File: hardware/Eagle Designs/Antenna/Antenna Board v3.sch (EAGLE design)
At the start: 12 parts, among them J10 U.FL-R-SMT-1(01), J11 U.FL-R-SMT-1(01), J12 U.FL-R-SMT-1(01), J2 MOLEX_503763-0491MOLEX_503763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, J3 MOLEX_503763-0491MOLEX_503763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, J4 MOLEX_503763-0291MOLEX_503763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, J6 MOLEX_503763-0491MOLEX_503763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, J7 MOLEX_503763-0491MOLEX_503763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, J8 MOLEX_503763-0291MOLEX_503763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, J9 MOLEX_503763-0291MOLEX_503763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

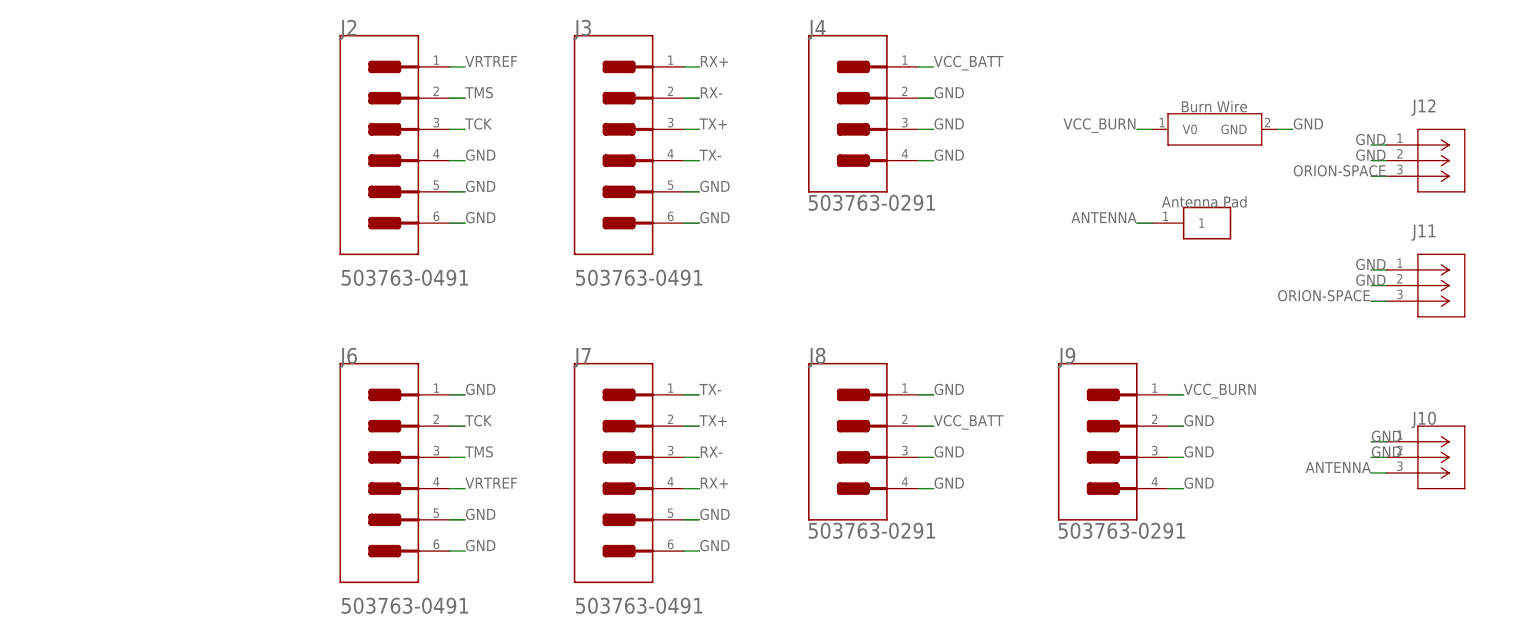
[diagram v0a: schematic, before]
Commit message: Added antenna board v3, removed extra antenna board v2 files
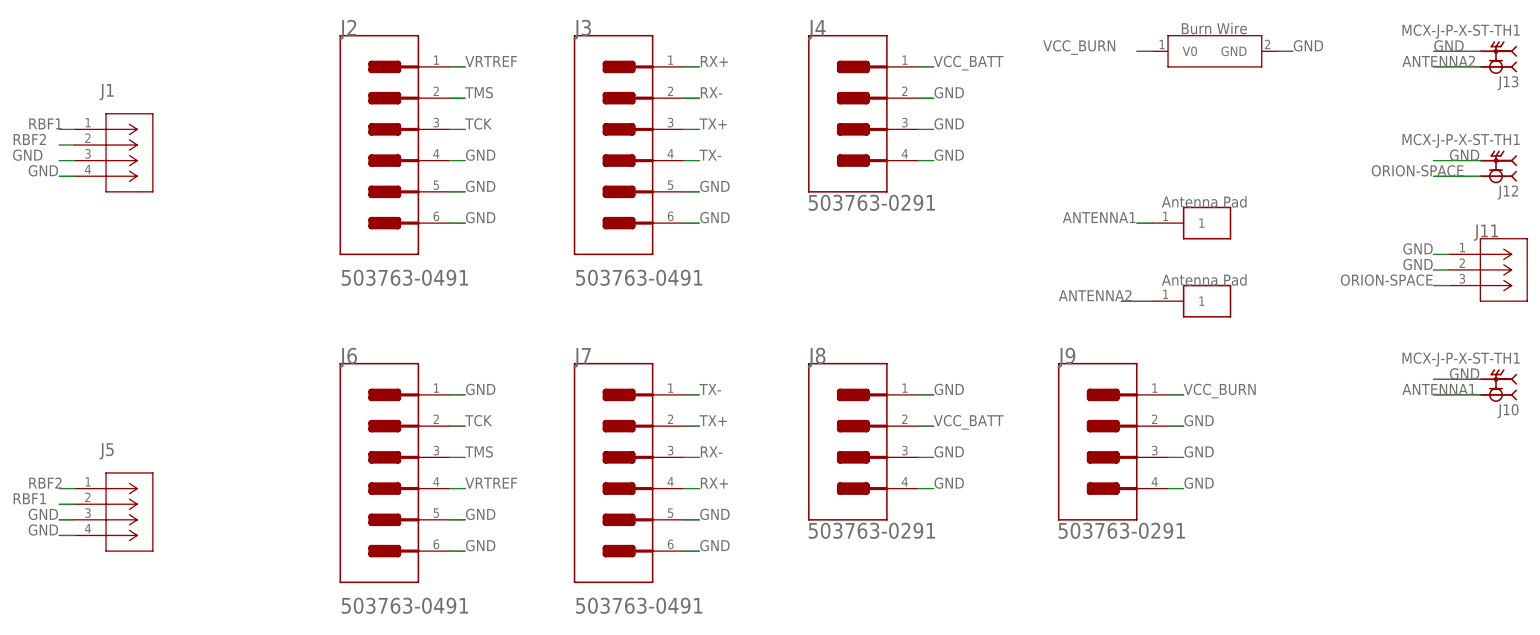
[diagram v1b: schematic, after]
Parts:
- added J1, J5: 5037630291, Molex_503763-0291:5037630291
- added J13: MCX-J-P-X-ST-TH1, MCX-J-P-X-ST-TH1:MCX-J-P-X-ST-TH1
- added U$1: ANTENNA_PAD, Antenna_Pad:ANTENNA_PAD
- J10: value U.FL-R-SMT-1(01) -> MCX-J-P-X-ST-TH1; device U.FL-R-SMT-1(01):U.FL-R-SMT-1(01) -> MCX-J-P-X-ST-TH1:MCX-J-P-X-ST-TH1
- J11: device U.FL-R-SMT:U.FL-R-SMT-1(01) -> U.FL-R-SMT-1(01):U.FL-R-SMT-1(01)
- J12: value U.FL-R-SMT-1(01) -> MCX-J-P-X-ST-TH1; device U.FL-R-SMT:U.FL-R-SMT-1(01) -> MCX-J-P-X-ST-TH1:MCX-J-P-X-ST-TH1
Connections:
- removed net ANTENNA: J10.3, U$2.1
- new net ANTENNA1: J10.1, U$2.1
- new net ANTENNA2: J13.1, U$1.1
- new net RBF1: J1.1, J5.2
- new net RBF2: J1.2, J5.1
- net GND: now also J1.3, J1.4, J13.2, J5.3, J5.4; no longer J10.1, J12.1
- net ORION-SPACE: now also J12.1; no longer J12.3
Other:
- moved on the sheet: J11
